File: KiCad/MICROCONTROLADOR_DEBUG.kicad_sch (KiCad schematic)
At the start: 7 parts, among them U3 PIC24HJ128GP502-I_SO, Y1 8MHz

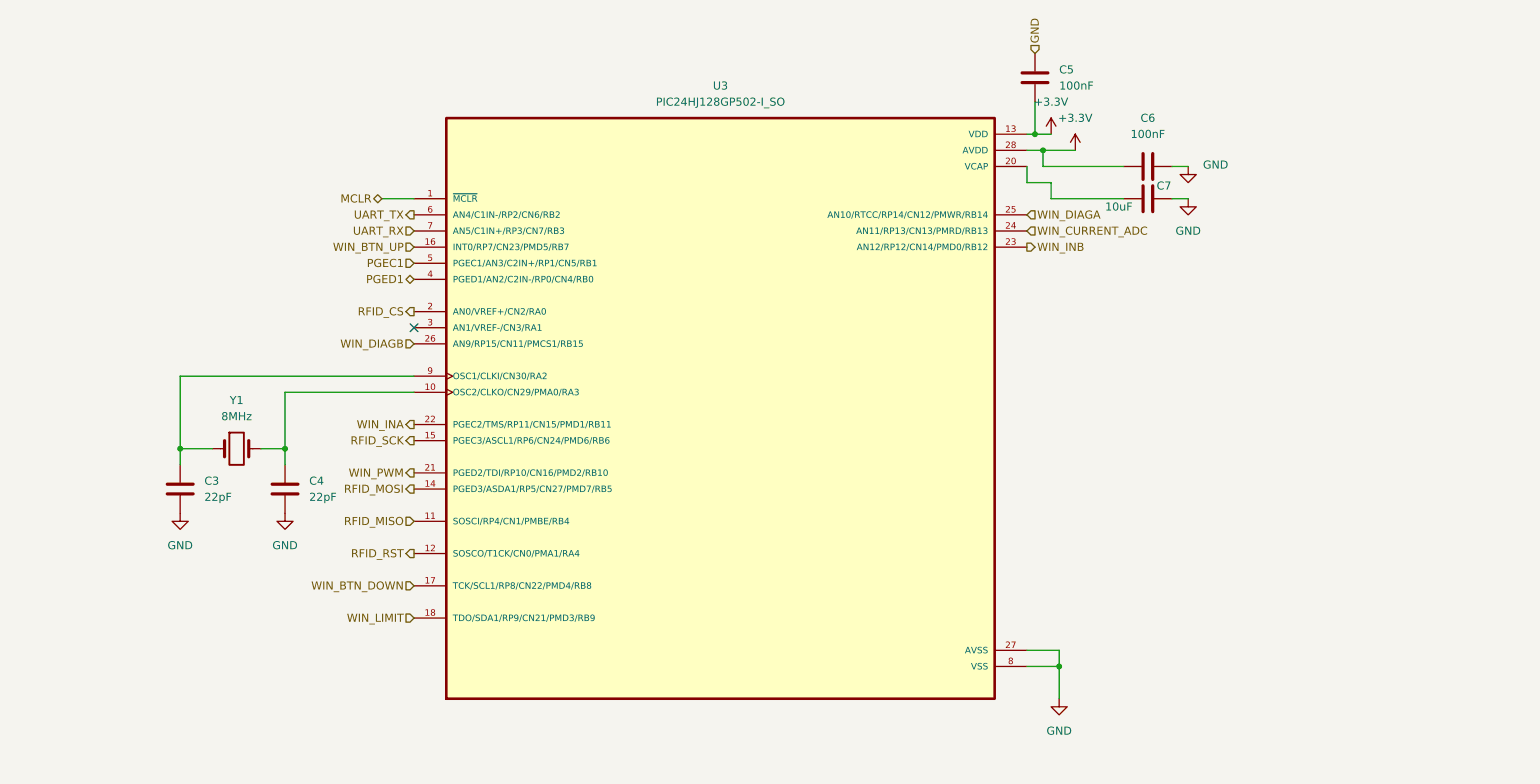
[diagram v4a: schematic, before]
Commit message: Update del nou Microcontrolador
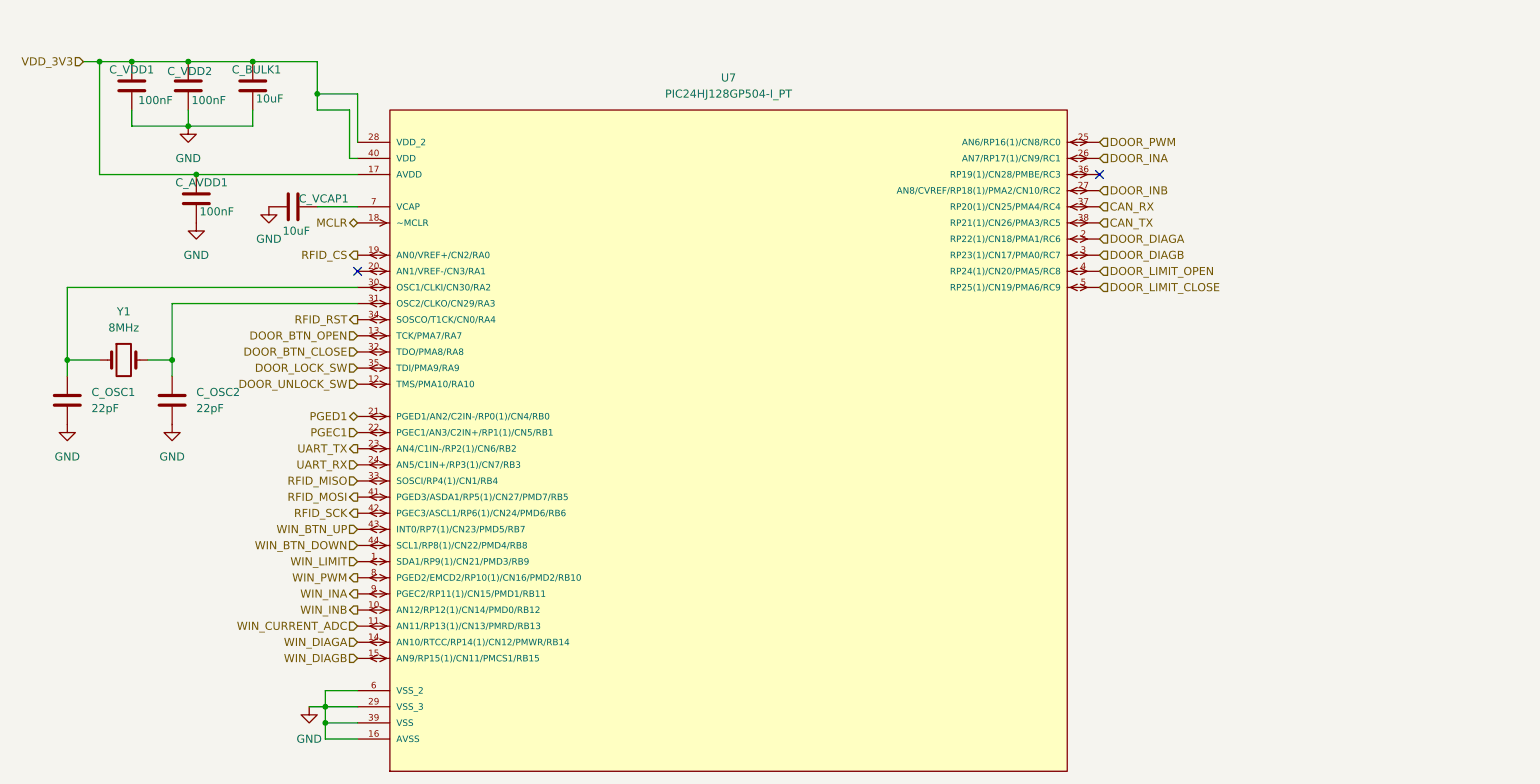
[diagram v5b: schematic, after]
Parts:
- removed C5, C6: 100nF, symbol Device:C
- removed C7: 10uF, symbol Device:C
- removed U3: PIC24HJ128GP502-I_SO, PIC24HJ128GP502-I_SO:SOIC127P1030X265-28N, symbol PIC24HJ128GP502-I_SO:PIC24HJ128GP502-I_SO
- added C_AVDD1, C_VDD1, C_VDD2: 100nF, Capacitor_SMD:C_0603_1608Metric, symbol Device:C
- added C_BULK1: 10uF, Capacitor_SMD:C_0805_2012Metric, symbol Device:C
- added C_VCAP1: 10uF, Capacitor_SMD:C_1206_3216Metric, symbol Device:C
- added U7: PIC24HJ128GP504-I_PT, PIC24HJ128GP504-I_PT:QFP80P1200X1200X120-44N, symbol PIC24HJ128GP504-I_PT:PIC24HJ128GP504-I_PT
- C_OSC1: renamed from C3; footprint (none) -> Capacitor_SMD:C_0603_1608Metric
- C_OSC2: renamed from C4; footprint (none) -> Capacitor_SMD:C_0603_1608Metric
- Y1: footprint Crystal:Crystal_SMD_3225-4Pin_3.2x2.5mm -> Crystal:Crystal_HC49-U_Horizontal
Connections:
- net GND: now also C_AVDD1.2, C_BULK1.2, C_VCAP1.2, C_VDD1.2, C_VDD2.2, U7.16 (AVSS), U7.29 (VSS_3), U7.39 (VSS), U7.6 (VSS_2)
- net MCLR: now also U7.18 (~MCLR)
- net PGEC1: now also U7.22 (PGEC1/AN3/C2IN+/RP1(1)/CN5/RB1)
- net PGED1: now also U7.21 (PGED1/AN2/C2IN-/RP0(1)/CN4/RB0)
- net RFID_CS: now also U7.19 (AN0/VREF+/CN2/RA0)
- net RFID_MISO: now also U7.33 (SOSCI/RP4(1)/CN1/RB4)
- net RFID_MOSI: now also U7.41 (PGED3/ASDA1/RP5(1)/CN27/PMD7/RB5)
- net RFID_RST: now also U7.34 (SOSCO/T1CK/CN0/RA4)
- net RFID_SCK: now also U7.42 (PGEC3/ASCL1/RP6(1)/CN24/PMD6/RB6)
- net UART_RX: now also U7.24 (AN5/C1IN+/RP3(1)/CN7/RB3)
- net UART_TX: now also U7.23 (AN4/C1IN-/RP2(1)/CN6/RB2)
- net WIN_BTN_DOWN: now also U7.44 (SCL1/RP8(1)/CN22/PMD4/RB8)
- net WIN_BTN_UP: now also U7.43 (INT0/RP7(1)/CN23/PMD5/RB7)
- net WIN_CURRENT_ADC: now also U7.11 (AN11/RP13(1)/CN13/PMRD/RB13)
- net WIN_DIAGA: now also U7.14 (AN10/RTCC/RP14(1)/CN12/PMWR/RB14)
- net WIN_DIAGB: now also U7.15 (AN9/RP15(1)/CN11/PMCS1/RB15)
- net WIN_INA: now also U7.9 (PGEC2/RP11(1)/CN15/PMD1/RB11)
- net WIN_INB: now also U7.10 (AN12/RP12(1)/CN14/PMD0/RB12)
- net WIN_LIMIT: now also U7.1 (SDA1/RP9(1)/CN21/PMD3/RB9)
- net WIN_PWM: now also U7.8 (PGED2/EMCD2/RP10(1)/CN16/PMD2/RB10)
- net at C_OSC2.1, Y1.2: now also U7.31 (OSC2/CLKO/CN29/RA3)
- net at C_OSC1.1, Y1.1: now also U7.30 (OSC1/CLKI/CN30/RA2)
- new net: C_VCAP1.1, U7.7 (VCAP)
- new net CAN_RX: U7.37 (RP20(1)/CN25/PMA4/RC4)
- new net CAN_TX: U7.38 (RP21(1)/CN26/PMA3/RC5)
- new net DOOR_BTN_CLOSE: U7.32 (TDO/PMA8/RA8)
- new net DOOR_BTN_OPEN: U7.13 (TCK/PMA7/RA7)
- new net DOOR_DIAGA: U7.2 (RP22(1)/CN18/PMA1/RC6)
- new net DOOR_DIAGB: U7.3 (RP23(1)/CN17/PMA0/RC7)
- new net DOOR_INA: U7.26 (AN7/RP17(1)/CN9/RC1)
- new net DOOR_INB: U7.27 (AN8/CVREF/RP18(1)/PMA2/CN10/RC2)
- new net DOOR_LIMIT_CLOSE: U7.5 (RP25(1)/CN19/PMA6/RC9)
- new net DOOR_LIMIT_OPEN: U7.4 (RP24(1)/CN20/PMA5/RC8)
- new net DOOR_LOCK_SW: U7.35 (TDI/PMA9/RA9)
- new net DOOR_PWM: U7.25 (AN6/RP16(1)/CN8/RC0)
- new net DOOR_UNLOCK_SW: U7.12 (TMS/PMA10/RA10)
- new net VDD_3V3: C_AVDD1.1, C_BULK1.1, C_VDD1.1, C_VDD2.1, U7.17 (AVDD), U7.28 (VDD_2), U7.40 (VDD)
- no-connect marks 1 -> 2
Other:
- moved on the sheet: C_OSC1, C_OSC2, Y1

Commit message: Versió final Esquematic
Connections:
- net DOOR_BTN_CLOSE renamed DOOR_BTN_CLOSED
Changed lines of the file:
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@@
 	)
 	(hierarchical_label "DOOR_INB"
-		(shape input)
+		(shape output)
 		(at 210.82 48.26 0)
 		(effects
@@
 		)
 	)
-	(hierarchical_label "DOOR_BTN_CLOSE"
+	(hierarchical_label "DOOR_BTN_CLOSED"
 		(shape input)
 		(at 93.98 73.66 180)
@@
 	)
 	(hierarchical_label "CAN_TX"
-		(shape input)
+		(shape output)
 		(at 210.82 53.34 0)
 		(effects
@@
 	)
 	(hierarchical_label "DOOR_INA"
-		(shape input)
+		(shape output)
 		(at 210.82 43.18 0)
 		(effects
@@
 	)
 	(hierarchical_label "DOOR_PWM"
-		(shape input)
+		(shape output)
 		(at 210.82 40.64 0)
 		(effects

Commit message: Versió final de l'esquematic
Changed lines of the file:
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@@
+		(color 0 0 0 0)
+	)
+	(junction
+		(at 88.9 130.81)
+		(diameter 0)
 		(color 0 0 0 0)
 	)
@@
 	(wire
 		(pts
+			(xy 88.9 129.54) (xy 88.9 130.81)
+		)
+		(stroke
+			(width 0)
+			(type default)
+		)
+	)
+	(wire
+		(pts
+			(xy 87.63 33.02) (xy 87.63 35.56)
+		)
+		(stroke
+			(width 0)
+			(type default)
+		)
+	)
+	(wire
+		(pts
+			(xy 53.34 27.94) (xy 58.42 27.94)
+		)
+		(stroke
+			(width 0)
+			(type default)
+		)
+	)
+	(wire
+		(pts
+			(xy 87.63 33.02) (xy 93.98 33.02)
+		)
+		(stroke
+			(width 0)
+			(type default)
+		)
+	)
+	(wire
+		(pts
+			(xy 77.47 38.1) (xy 77.47 35.56)
+		)
+		(stroke
+			(width 0)
+			(type default)
+		)
+	)
+	(wire
+		(pts
+			(xy 60.96 74.93) (xy 64.77 74.93)
+		)
+		(stroke
+			(width 0)
+			(type default)
+		)
+	)
+	(wire
+		(pts
+			(xy 67.31 27.94) (xy 77.47 27.94)
+		)
+		(stroke
+			(width 0)
+			(type default)
+		)
+	)
+	(wire
+		(pts
+			(xy 48.26 74.93) (xy 48.26 77.47)
+		)
+		(stroke
+			(width 0)
+			(type default)
+		)
+	)
+	(wire
+		(pts
+			(xy 93.98 134.62) (xy 88.9 134.62)
+		)
+		(stroke
+			(width 0)
+			(type default)
+		)
+	)
+	(wire
+		(pts
+			(xy 68.58 45.72) (xy 93.98 45.72)
+		)
+		(stroke
+			(width 0)
+			(type default)
+		)
+	)
+	(wire
+		(pts
+			(xy 50.8 27.94) (xy 53.34 27.94)
+		)
+		(stroke
+			(width 0)
+			(type default)
+		)
+	)
+	(wire
+		(pts
 			(xy 88.9 132.08) (xy 93.98 132.08)
 		)
@@
 	(wire
 		(pts
-			(xy 88.9 129.54) (xy 88.9 132.08)
-		)
-		(stroke
-			(width 0)
-			(type default)
-		)
-	)
-	(wire
-		(pts
-			(xy 87.63 33.02) (xy 87.63 35.56)
-		)
-		(stroke
-			(width 0)
-			(type default)
-		)
-	)
-	(wire
-		(pts
-			(xy 53.34 27.94) (xy 58.42 27.94)
-		)
-		(stroke
-			(width 0)
-			(type default)
-		)
-	)
-	(wire
-		(pts
-			(xy 87.63 33.02) (xy 93.98 33.02)
-		)
-		(stroke
-			(width 0)
-			(type default)
-		)
-	)
-	(wire
-		(pts
-			(xy 88.9 134.62) (xy 88.9 132.08)
-		)
-		(stroke
-			(width 0)
-			(type default)
-		)
-	)
-	(wire
-		(pts
-			(xy 77.47 38.1) (xy 77.47 35.56)
-		)
-		(stroke
-			(width 0)
-			(type default)
-		)
-	)
-	(wire
-		(pts
-			(xy 60.96 74.93) (xy 64.77 74.93)
-		)
-		(stroke
-			(width 0)
-			(type default)
-		)
-	)
-	(wire
-		(pts
-			(xy 67.31 27.94) (xy 77.47 27.94)
-		)
-		(stroke
-			(width 0)
-			(type default)
-		)
-	)
-	(wire
-		(pts
-			(xy 86.36 129.54) (xy 88.9 129.54)
-		)
-		(stroke
-			(width 0)
-			(type default)
-		)
-	)
-	(wire
-		(pts
-			(xy 48.26 74.93) (xy 48.26 77.47)
-		)
-		(stroke
-			(width 0)
-			(type default)
-		)
-	)
-	(wire
-		(pts
-			(xy 93.98 134.62) (xy 88.9 134.62)
-		)
-		(stroke
-			(width 0)
-			(type default)
-		)
-	)
-	(wire
-		(pts
-			(xy 68.58 45.72) (xy 93.98 45.72)
-		)
-		(stroke
-			(width 0)
-			(type default)
-		)
-	)
-	(wire
-		(pts
-			(xy 50.8 27.94) (xy 53.34 27.94)
-		)
-		(stroke
-			(width 0)
-			(type default)
-		)
-	)
-	(wire
-		(pts
 			(xy 48.26 63.5) (xy 48.26 74.93)
 		)
@@
 	(wire
 		(pts
+			(xy 88.9 130.81) (xy 88.9 132.08)
+		)
+		(stroke
+			(width 0)
+			(type default)
+		)
+	)
+	(wire
+		(pts
 			(xy 64.77 66.04) (xy 64.77 74.93)
 		)
@@
 	(wire
 		(pts
+			(xy 86.36 130.81) (xy 88.9 130.81)
+		)
+		(stroke
+			(width 0)
+			(type default)
+		)
+	)
+	(wire
+		(pts
 			(xy 93.98 66.04) (xy 64.77 66.04)
 		)
@@
 		(pts
 			(xy 92.71 35.56) (xy 92.71 43.18)
+		)
+		(stroke
+			(width 0)
+			(type default)
+		)
+	)
+	(wire
+		(pts
+			(xy 88.9 132.08) (xy 88.9 134.62)
 		)
 		(stroke
@@
 	(symbol
 		(lib_id "power:GND")
-		(at 86.36 129.54 0)
+		(at 86.36 130.81 0)
 		(unit 1)
 		(exclude_from_sim no)
@@
 		(fields_autoplaced yes)
 		(property "Reference" "#PWR045"
+			(at 86.36 137.16 0)
+			(effects
+				(font
+					(size 1.27 1.27)
+				)
+				(hide yes)
+			)
+		)
+		(property "Value" "GND"
 			(at 86.36 135.89 0)
 			(effects
@@
 					(size 1.27 1.27)
 				)
-				(hide yes)
-			)
-		)
-		(property "Value" "GND"
-			(at 86.36 134.62 0)
-			(effects
-				(font
-					(size 1.27 1.27)
-				)
 			)
 		)
 		(property "Footprint" ""
-			(at 86.36 129.54 0)
+			(at 86.36 130.81 0)
 			(effects
 				(font
@@
 		)
 		(property "Datasheet" ""
-			(at 86.36 129.54 0)
+			(at 86.36 130.81 0)
 			(effects
 				(font
@@
 		)
 		(property "Description" "Power symbol creates a global label with name \"GND\" , ground"
-			(at 86.36 129.54 0)
-			(effects
-				(font
+			(at 86.36 130.81 0)
+			(effects
+				(font

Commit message: 1ra versióPCB
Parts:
- Y1: footprint Crystal:Crystal_HC49-U_Horizontal -> Crystal:Crystal_SMD_3225-4Pin_3.2x2.5mm
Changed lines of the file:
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@@
 			)
 		)
-		(property "Footprint" "Crystal:Crystal_HC49-U_Horizontal"
+		(property "Footprint" "Crystal:Crystal_SMD_3225-4Pin_3.2x2.5mm"
 			(at 57.15 74.93 0)
 			(effects
